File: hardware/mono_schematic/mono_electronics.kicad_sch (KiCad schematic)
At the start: 0 parts

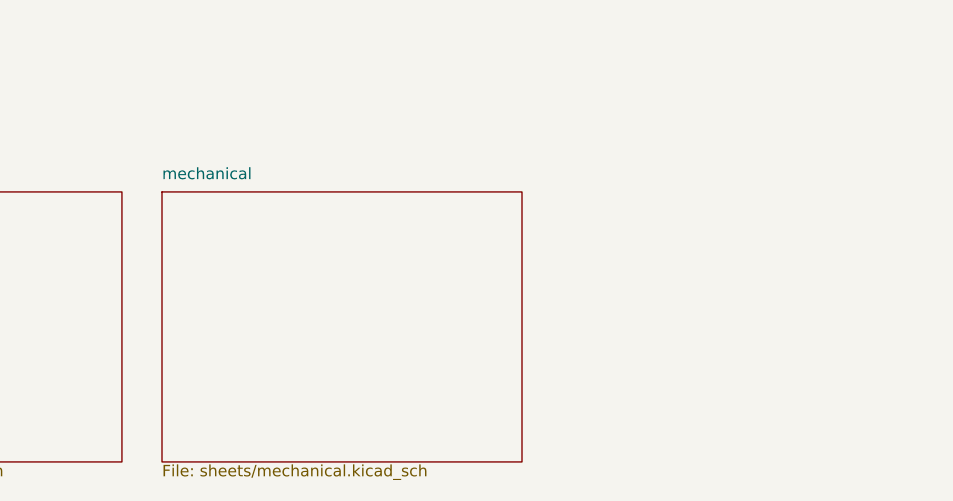
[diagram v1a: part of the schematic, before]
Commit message: mono_electronics v12: LED interface standard on FFC spares (ID I2C 33R+PESD5V0S2BT, ID_3V3 100R, GND 33/38/40; DNP column-expansion taps incl. U_LED2 SDO), schematic regen (ERC 0, 0 diffs), fab v12; garland 480 Hz scan mode (scan_div) + timing fix
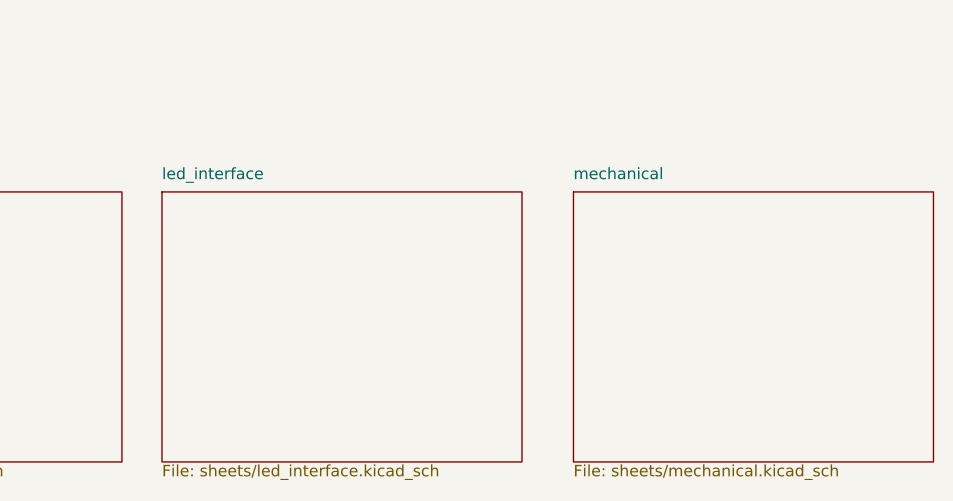
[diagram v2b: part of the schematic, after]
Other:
- added sheet led_interface (sheets/led_interface.kicad_sch)
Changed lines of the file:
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@@
       (type none)
     )
-    (property "Sheetname" "mechanical"
+    (property "Sheetname" "led_interface"
       (at 389.89 58.42 0)
       (effects
@@
       )
     )
-    (property "Sheetfile" "sheets/mechanical.kicad_sch"
+    (property "Sheetfile" "sheets/led_interface.kicad_sch"
       (at 389.89 91.44 0)
       (effects
         (font
+          (size 1.27 1.27)
+        )
+        (justify left bottom)
+      )
+    )
+  )
+  (sheet
+    (at 435.61 59.69)
+    (size 40 30)
+    (fields_autoplaced yes)
+    (stroke
+      (width 0.1524)
+      (type solid)
+    )
+    (fill
+      (type none)
+    )
+    (property "Sheetname" "mechanical"
+      (at 435.61 58.42 0)
+      (effects
+        (font
+          (size 1.27 1.27)
+        )
+        (justify left bottom)
+      )
+    )
+    (property "Sheetfile" "sheets/mechanical.kicad_sch"
+      (at 435.61 91.44 0)
+      (effects
+        (font
